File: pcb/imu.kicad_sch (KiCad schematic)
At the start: 3 parts, among them U6 LSM6DSV

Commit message: Simplify to minimum buck converter components
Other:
- title: (none) -> LMP91000 Portable Potentiostat
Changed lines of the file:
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@@
 	(generator_version "9.0")
 	(paper "A4")
+	(title_block
+		(title "LMP91000 Portable Potentiostat")
+	)
 	(rectangle
 		(start 12.7 50.8)

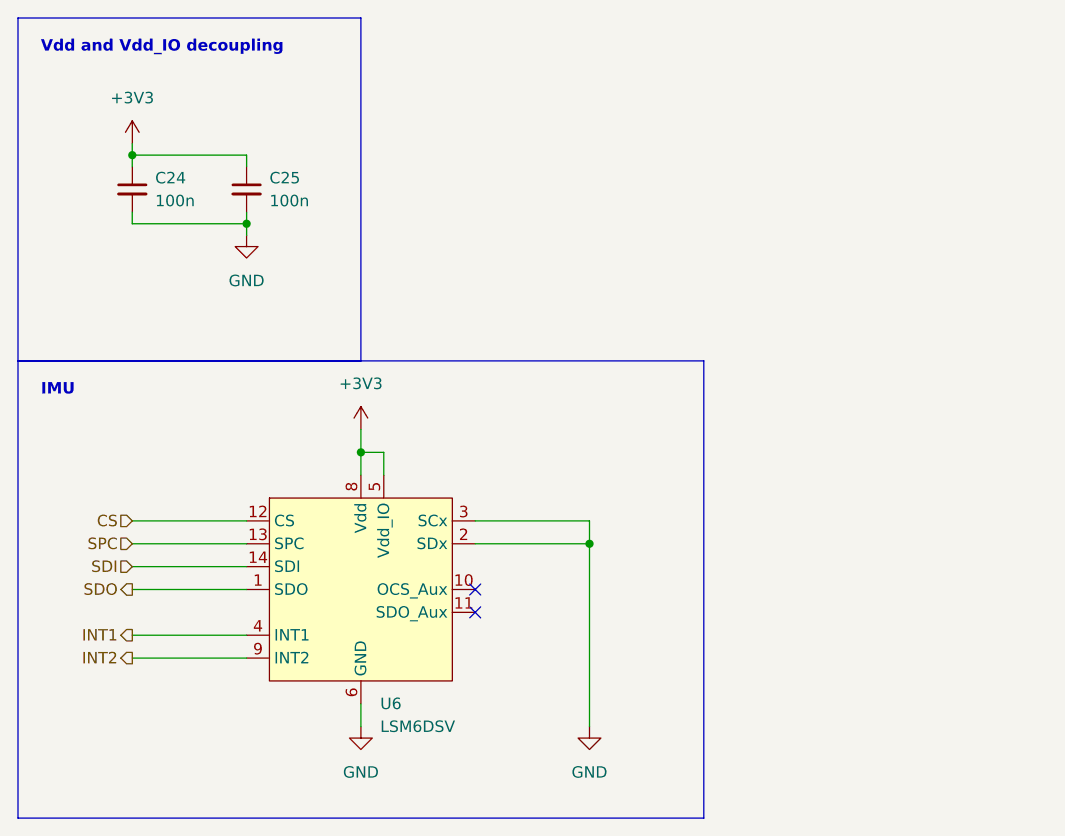
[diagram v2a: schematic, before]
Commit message: Assign footprints, cleanup schematics, start layout
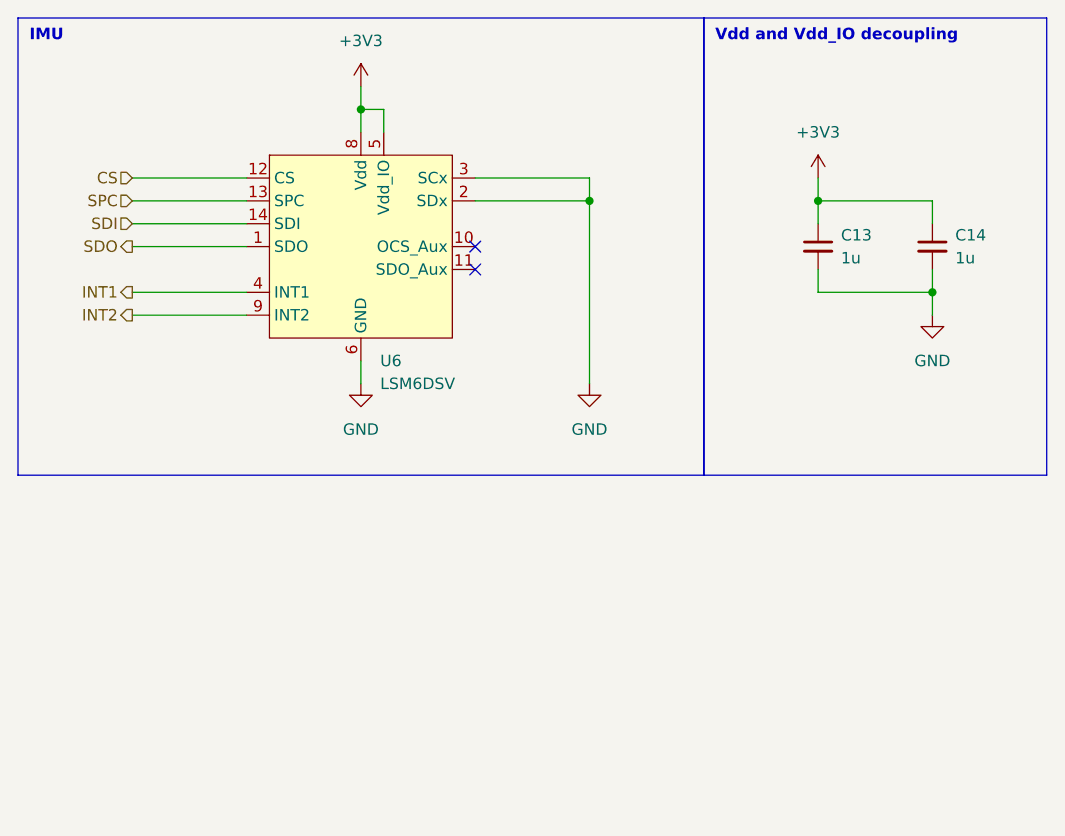
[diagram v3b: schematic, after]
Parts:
- C13: renamed from C24; value 100n -> 1u; footprint (none) -> Capacitor_SMD:C_0402_1005Metric
- C14: renamed from C25; value 100n -> 1u; footprint (none) -> Capacitor_SMD:C_0402_1005Metric
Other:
- company: (none) -> Clarkson University
- moved on the sheet: C13, C14, U6

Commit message: Move antenna and tag connect
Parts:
- C13, C14: HQ_MPN (none) -> CL05X105KP5NNNC
- U6: HQ_MPN (none) -> LSM6DSVTR
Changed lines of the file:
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@@
+			)
+		)
+		(property "HQ_MPN" "LSM6DSVTR"
+			(at 50.8 25.4 0)
+			(effects
+				(font
+					(size 1.27 1.27)
+				)
+				(hide yes)
 			)
 		)
@@
 			)
 		)
+		(property "HQ_MPN" "CL05X105KP5NNNC"
+			(at 101.6 38.1 0)
+			(effects
+				(font
+					(size 1.27 1.27)
+				)
+				(hide yes)
+			)
+		)
 		(pin "1"
 		)
@@
 			(at 114.3 38.1 0)
 			(effects
+				(font
+					(size 1.27 1.27)
+				)
+				(hide yes)
+			)
+		)
+		(property "HQ_MPN" "CL05X105KP5NNNC"
+			(at 114.3 38.1 0)
+			(effects
